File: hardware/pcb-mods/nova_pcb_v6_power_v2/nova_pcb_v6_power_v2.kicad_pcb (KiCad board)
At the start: 4 copper layers, 112 x 90 mm, 55 parts, among them J1 XT60_4S_IN, J12 XT30_JET_12V, J13 XT30_L2_12V, J2 UBEC_5V_AUX, J20 IB_2x06, J3 XT30_Inj, J4 XT30_Inj, J5 XT30_Inj, J6 XT30_Inj, J7 XT30_Inj, J8 ServoBus_TTL, M1 Voltmeter_DC, Q1 IRLB3034PBF, Q2 BSS138_cutoff, Q3 BSS138_estop, Q4 BSS138_jetcut, SW1 Rocker_30A, SW2 Estop_NC_latching, U1 Pololu_D42V110F7_LEG_7V5, U10 INA226, U11 INA226, U2 Pololu_D42V110F12_HIP_12V, U3 Pololu_D24V22F12_L2_12V, U4 Pololu_D42V55F12_JET_12V, U5 Pololu_D42V55F7_ARM_7V5, U8 LM393, U9 INA226

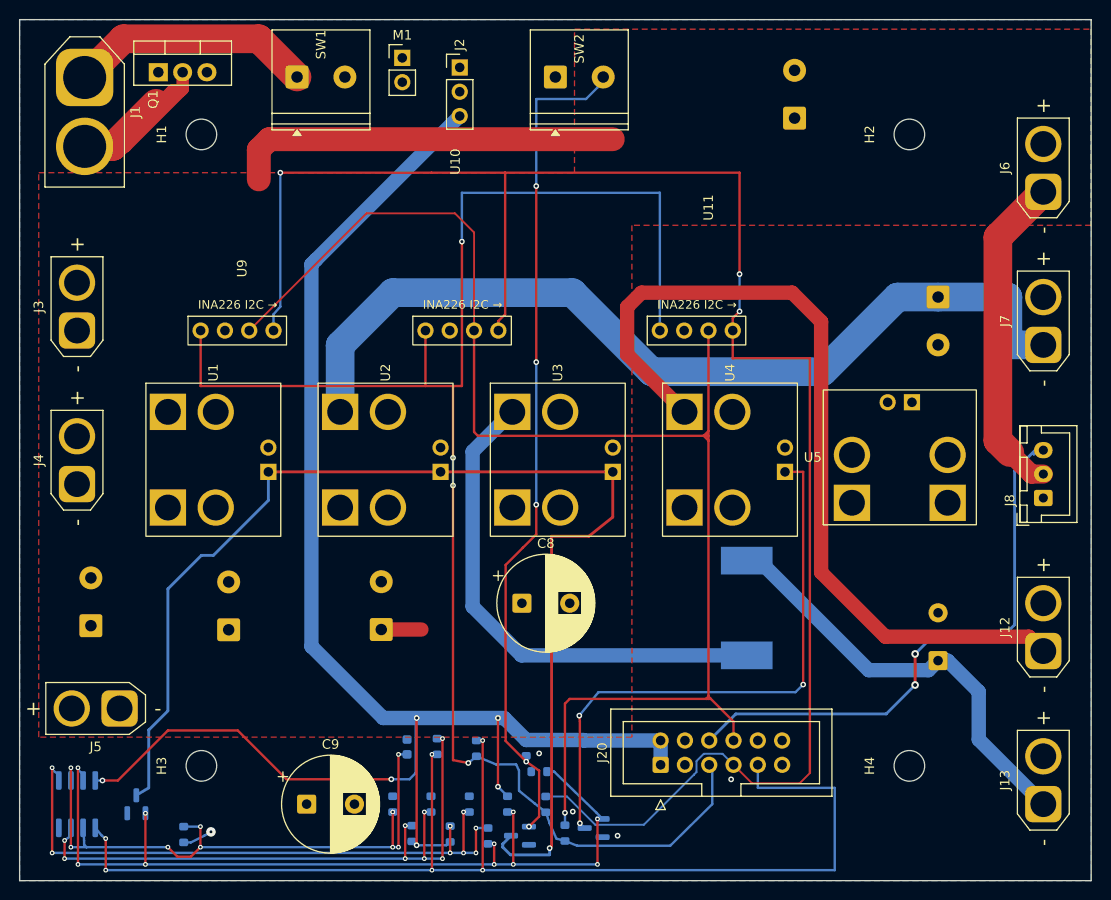
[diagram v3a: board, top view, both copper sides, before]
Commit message: power board: arm Phase-4 routed + cleaned + fresh gerbers (fab-ready) (#13)
Completes the power board (blocker B1):
- U5.EN routed on EN_BUCKS (re-gate now realized on the board).
- V7V5_ARM 3mm, BATT_NEG/VBAT long runs 3mm, 21 high-current pads solid
  zone-connection (current-capacity fixes; TO-220/SW1 escapes left at 1.3mm).
- Removed the duplicate U12 + J14 (F8 UUID-mismatch artifacts) and the full
  orphan dangling-track chain they left behind.
- DRC: 0 hard, 0 unconnected, 0 dangling (10 cosmetic silk/lib only).
- Gerbers regenerated; fab_gate GO on both boards (J20 cross-board match OK).

DNP roster correct (U5 arm buck, U12 arm INA = Phase-4 reserve).

Co-authored-by: Claude Opus 4.8 <noreply@anthropic.com>
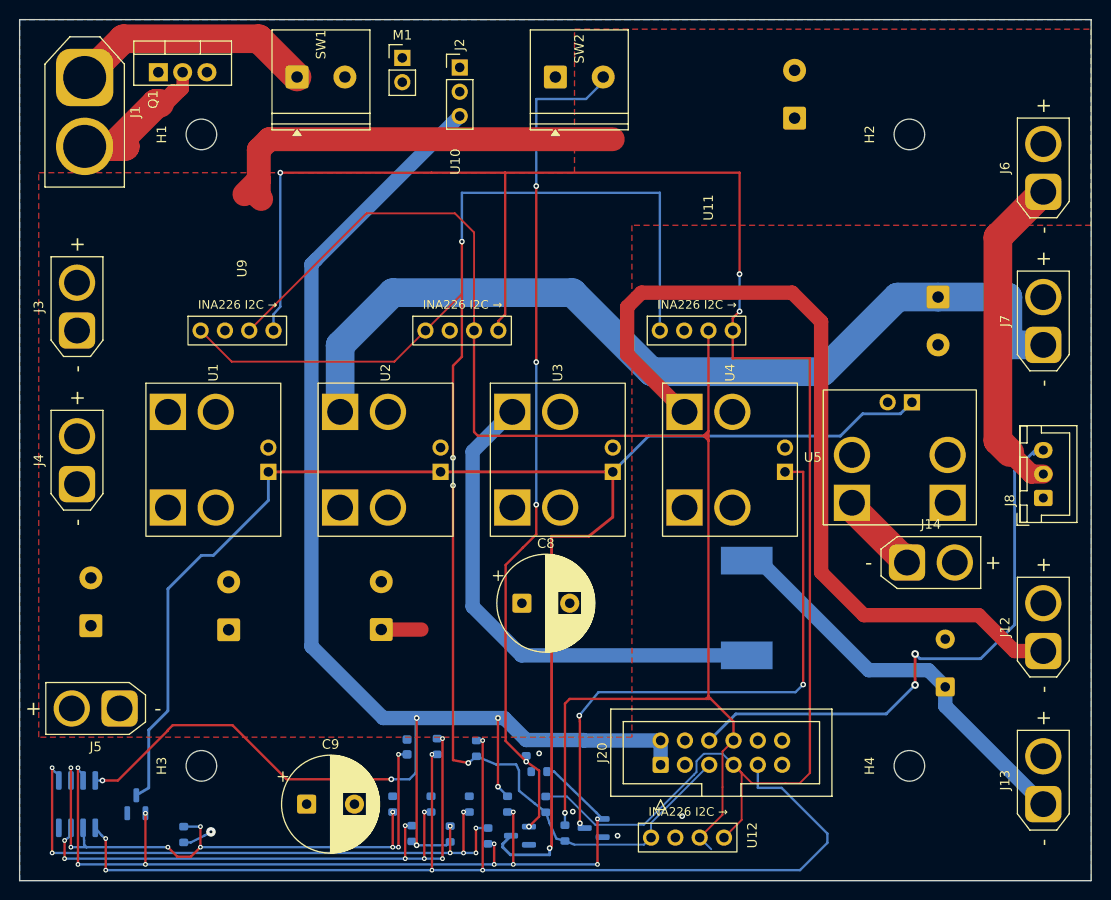
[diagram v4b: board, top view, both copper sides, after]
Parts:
- added J14: XT30_Arm7V5, Connector_AMASS:AMASS_XT30U-M_1x02_P5.0mm_Vertical, F.Cu at (176.8, 107.8)
- added U12: INA226, nova_v6:INA226_Module_Breakout, F.Cu at (155.1, 130.0)
- moved C6 2.85 mm to (180.8, 120.8)
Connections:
- U5 pad 3: VBAT_PROTECTED -> EN_BUCKS
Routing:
- net EN_BUCKS: track 128.5 -> 162.7 mm
- net I2C_SCL: track 149.4 -> 162.8 mm
- net I2C_SDA: track 187.0 -> 196.2 mm
- net V7V5_ARM: track 0.00 -> 9.13 mm
- net +3V3: track 172.1 -> 163.8 mm
- net BATT_LOW: track 127.0 -> 121.0 mm
- net V7V5_LEG: track 78.9 -> 83.2 mm
- net V12_L2: track 45.3 -> 42.7 mm

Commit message: boards: fab-ready GO (both) — Q1 gate-harden + soft-start, mounting-hole keepouts, BATT_NEG zone, PWR_FLAG, fresh gerbers (separate NPTH/PTH)
Power v2: Q1 gate soft-start (R17 10k + C_gs 470nF + D1 18V zener + R_gs) on Q1_GATE,
BATT_NEG F.Cu zone (solid to Q1 source, islands merged), 7mm copper keepout all 4 holes
all layers, GND PWR_FLAG. Logic: 7mm keepout all 4 holes (V5_AUX was 0.4mm from barrel).
Both: gerbers regenerated w/ explicit layer set + separate PTH/NPTH drill (M3 holes stay
non-plated). fab_gate GO: ERC 0 / DRC 0 hard / J20 match / DNP U5+U12.

Co-Authored-By: Claude Opus 4.8 <noreply@anthropic.com>
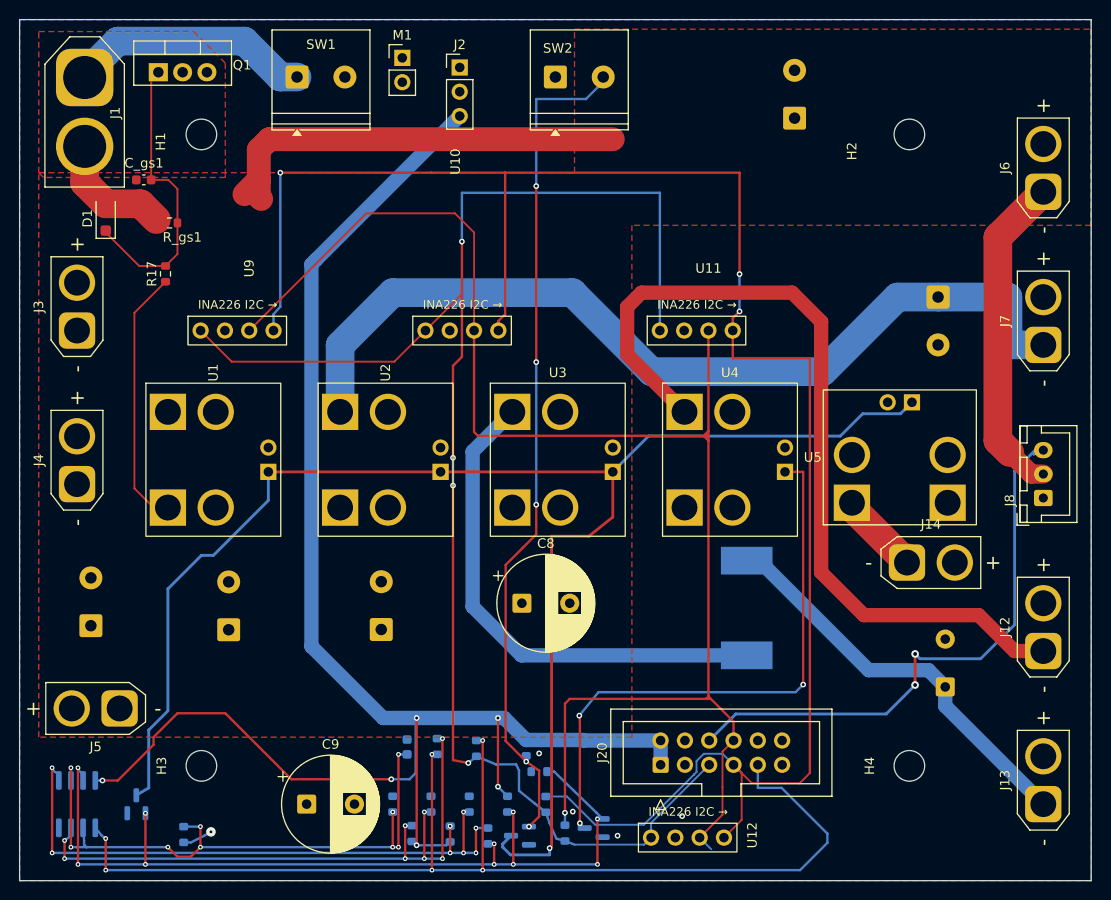
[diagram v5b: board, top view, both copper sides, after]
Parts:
- added C_gs1: 0.47μF, Capacitor_SMD:C_0603_1608Metric, F.Cu at (97.0, 67.8)
- added D1: BZT52C18 (18V), Diode_SMD:D_SOD-123F, F.Cu at (93.0, 71.7)
- added R17: 10k, Resistor_SMD:R_0603_1608Metric, F.Cu at (99.2, 77.6)
- added R_gs1: 100k, Resistor_SMD:R_0603_1608Metric, F.Cu at (99.7, 72.2)
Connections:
- Q1 pad 1: VBAT_PROTECTED -> Net-(D1-K)
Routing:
- net Net-(D1-K): track 0.00 -> 31.2 mm
- net VBAT_PROTECTED: track 3.12 -> 30.4 mm
- net /01 Battery Input + Reverse Protection/BATT_NEG: track 28.5 -> 12.9 mm
- net V7V5_LEG: track 83.2 -> 79.0 mm
- net V5_AUX: track 175.4 -> 176.9 mm
- added copper zone on F.Cu, net /01 Battery Input + Reverse Protection/BATT_NEG

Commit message: power board: SW1 drill 1.2→1.5mm (TB007) + close VBAT_PROTECTED reroute gap + regen gerbers
SW1 footprint drill 1.2→1.5mm for the TB007-508-02BE substitute (OOS MKDS
replacement; pin ~1.0mm, maker-rec Ø1.6 holes). SW2 left at 1.2 (kit block).

Closed an incomplete reroute on VBAT_PROTECTED (main protected rail) that left
the net open (DRC 1 unconnected): two 3mm stubs at X=95 joined by a vertical
3mm segment (95,82.75)->(95,99). Bundles prior uncommitted silk repositioning +
high-current trace widen. Zones refilled. DRC 0 hard / 0 unconnected,
fab_gate GO (both boards).

Co-Authored-By: Claude Opus 4.8 <noreply@anthropic.com>
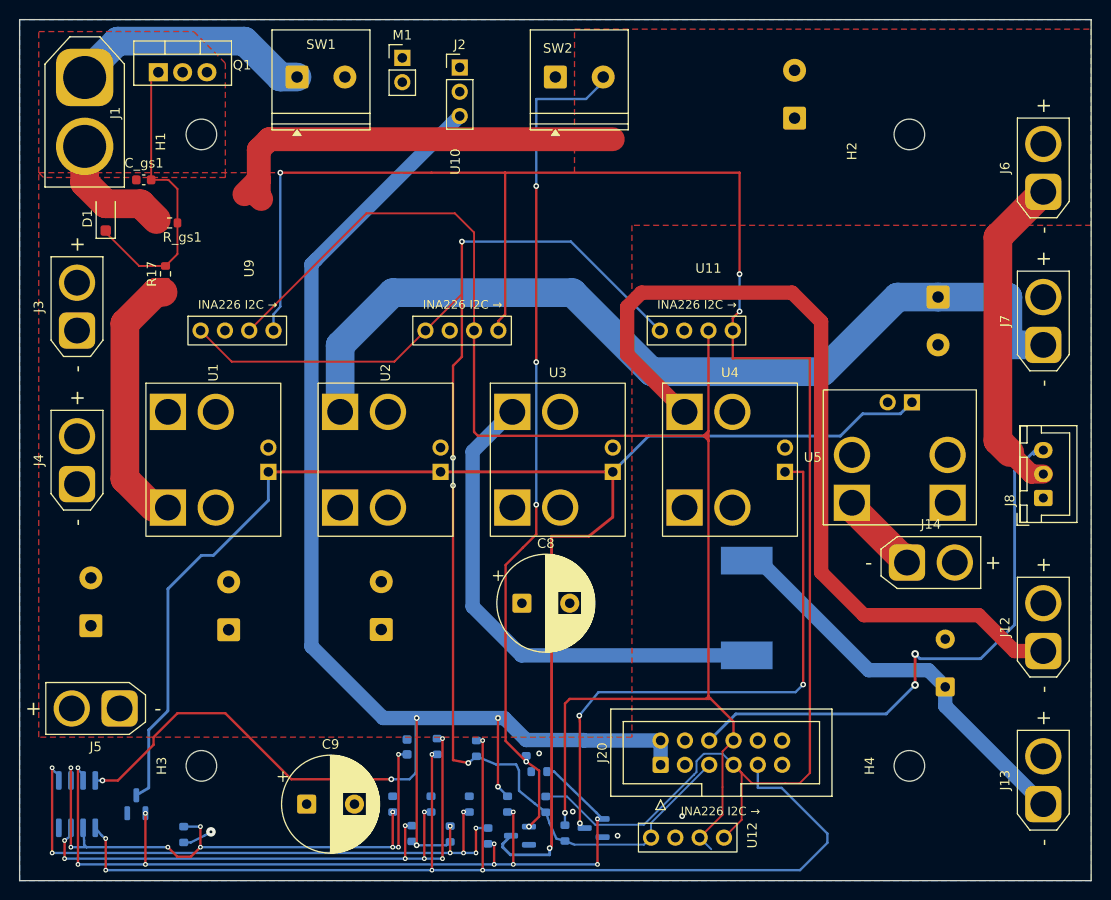
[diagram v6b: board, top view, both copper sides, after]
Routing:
- net +3V3: track 163.8 -> 148.2 mm
- net VBAT_PROTECTED: track 30.4 -> 31.7 mm
